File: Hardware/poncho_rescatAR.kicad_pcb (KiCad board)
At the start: 2 copper layers, 10 parts, among them P2 CONN_8, Q1 BC547

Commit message: retoques finales al esquemetico y pcb base
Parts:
- removed Q1: BC547, TO92
- removed R2: 10k, R4-LARGE_PADS
- removed R3: 680, R4-LARGE_PADS
- added BAT1: BAT_CONN, PIN_ARRAY_4x1, F.Cu at (165.3, 52.3)
- added C1: 10uF, C2V10, F.Cu at (163.9, 74.8)
- added C2: 10uF, C2V10, F.Cu at (92.2, 58.9)
- added C3: 0.1, C1, F.Cu at (162.4, 58.9)
- added C4: 0.1, C1, F.Cu at (157.3, 68.0)
- added C5: 0.1, C1, F.Cu at (103.5, 52.4)
- added C6: 0.1, C1, F.Cu at (99.5, 60.2)
- added P1: 5V_OUT, PINHEAD1-2, F.Cu at (85.2, 67.9)
- added R4: 470, R4-LARGE_PADS, F.Cu at (141.0, 62.8)
- added R5: 220, R4-LARGE_PADS, F.Cu at (150.8, 57.6)
- added U1: LM317T, TO220_VERT, F.Cu at (155.8, 62.8)
- added U2: LM7805, LM78XXV, F.Cu at (104.8, 59.0)
- CON_E-CIAA1, CON_E-CIAA2, CON_SO101, CON_SO104: footprint pin_strip_2mm_20x2 -> pin_strip_20x2
- D1: footprint LED-5MM -> LED-3MM
- P2: footprint pin_socket_2mm_8 -> pin_strip_8
- R1: value 330k -> 330
- moved R1 58.1 mm to (155.2, 85.3)
- moved D1 46.8 mm to (151.7, 91.2)
- moved P2 4.93 mm to (153.7, 109.6), turned to 270 degrees
- moved CON_E-CIAA2 4.24 mm to (90.5, 120.0)
- moved CON_E-CIAA1 3.73 mm to (161.6, 120.0)
- moved CON_SO104 2.25 mm to (122.0, 71.0)
- moved CON_SO101 2.18 mm to (122.0, 142.1), turned to 0 degrees
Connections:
- CON_E-CIAA1 pad 20: GND -> /GND
- CON_E-CIAA1 pad 22: GND -> /GND
- CON_E-CIAA1 pad 24: GND -> /GND
- CON_E-CIAA1 pad 26: GND -> /GND
- CON_E-CIAA1 pad 28: GND -> /GND
- CON_E-CIAA1 pad 30: GND -> /GND
- CON_E-CIAA1 pad 32: GND -> /GND
- CON_E-CIAA1 pad 38: GND -> /GND
- CON_E-CIAA1 pad 4: GND -> /GND
- CON_E-CIAA1 pad 40: GND -> /GND
- CON_E-CIAA2 pad 11: GND -> /GND
- CON_E-CIAA2 pad 13: GND -> /GND
- CON_E-CIAA2 pad 17: GND -> /GND
- CON_E-CIAA2 pad 19: GND -> /GND
- CON_E-CIAA2 pad 25: GND -> /GND
- CON_E-CIAA2 pad 27: GND -> /GND
- CON_E-CIAA2 pad 3: GND -> /GND
- CON_E-CIAA2 pad 37: GND -> /GND
- CON_E-CIAA2 pad 39: GND -> /GND
- CON_E-CIAA2 pad 5: GND -> /GND
- CON_E-CIAA2 pad 7: GND -> /GND
- CON_SO101 pad 11: GND -> /GND
- CON_SO101 pad 12: GND -> /GND
- CON_SO101 pad 13: GND -> /GND
- CON_SO101 pad 14: GND -> /GND
- CON_SO101 pad 19: GND -> /GND
- CON_SO101 pad 25: GND -> /GND
- CON_SO101 pad 26: GND -> /GND
- CON_SO101 pad 27: GND -> /GND
- CON_SO101 pad 28: GND -> /GND
- CON_SO101 pad 38: GND -> /GND
- CON_SO101 pad 39: GND -> /GND
- CON_SO101 pad 40: GND -> /GND
- CON_SO101 pad 5: GND -> /GND
- CON_SO104 pad 11: GND -> /GND
- CON_SO104 pad 12: GND -> /GND
- CON_SO104 pad 13: GND -> /GND
- CON_SO104 pad 14: GND -> /GND
- CON_SO104 pad 25: GND -> /GND
- CON_SO104 pad 26: GND -> /GND
- CON_SO104 pad 27: GND -> /GND
- CON_SO104 pad 28: GND -> /GND
- CON_SO104 pad 38: GND -> /GND
- CON_SO104 pad 39: GND -> /GND
- CON_SO104 pad 40: GND -> /GND
- CON_SO104 pad 5: GND -> /GND
- CON_SO104 pad 6: GND -> /GND
- CON_SO104 pad 7: GND -> /GND
- CON_SO104 pad 8: GND -> /GND
- D1 pad 1: /VCC_5V -> N-0000018
- D1 pad 2: N-000005 -> /STATUS_LED
- P2 pad 2: GND -> /GND
- P2 pad 7: GND -> /GND
- R1 pad 1: /STATUS_LED -> /VCC_3.8V
- R1 pad 2: GND -> N-0000018
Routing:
- net /VCC_5V: track 104.9 -> 0.00 mm
- net /VCC_3.8V: track 0.00 -> 104.1 mm
- net VCC: track 0.00 -> 72.6 mm
- net /RS232_RXD: track 98.9 -> 61.6 mm
- net /STATUS_LED: track 6.41 -> 37.3 mm
- net /RS232_TXD: track 42.4 -> 66.6 mm
- net N-000003: track 0.00 -> 21.8 mm
- net N-000002: track 0.00 -> 14.6 mm
- net /I2C_SCL: track 17.0 -> 28.6 mm
- net GND: track 10.5 -> 0.00 mm
- net N-000005: track 9.38 -> 0.00 mm
- net N-000007: track 5.64 -> 0.00 mm
- net /GE864_ON_OFF: track 99.8 -> 105.4 mm
- net N-000009: track 4.02 -> 0.00 mm
- net N-0000018: track 0.00 -> 3.63 mm
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
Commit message: perfeccionando el  pcb
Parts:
- C1, C2: footprint C2V10 -> C1V5
- moved C4 14.0 mm to (162.7, 55.1), turned to 90 degrees
- moved C1 13.1 mm to (163.9, 61.6), turned to 270 degrees
- moved R4 9.59 mm to (139.7, 53.2)
- moved R5 9.43 mm to (141.6, 60.0)
- moved C3 8.90 mm to (156.5, 52.3)
- moved U1 6.73 mm to (155.2, 56.0)
- moved BAT1 6.20 mm to (168.4, 57.6), turned to 270 degrees
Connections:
- U1 pad 2: VCC -> /VCC_3.8V
- U1 pad 3: /VCC_3.8V -> VCC
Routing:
- net /VCC_3.8V: track 104.1 -> 124.5 mm
- net /VCC_5V: track 0.00 -> 16.5 mm
- net N-000002: track 14.6 -> 22.3 mm
- net N-000003: track 21.8 -> 24.7 mm
- net VCC: track 72.6 -> 75.5 mm
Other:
- net class Default: clearance 0.7 -> 0.8
- net class Power added: clearance 0.8, trace_width 1, via_dia 0.889, via_drill 0.635
- rule trace_clearance: 0.7 -> 0.8

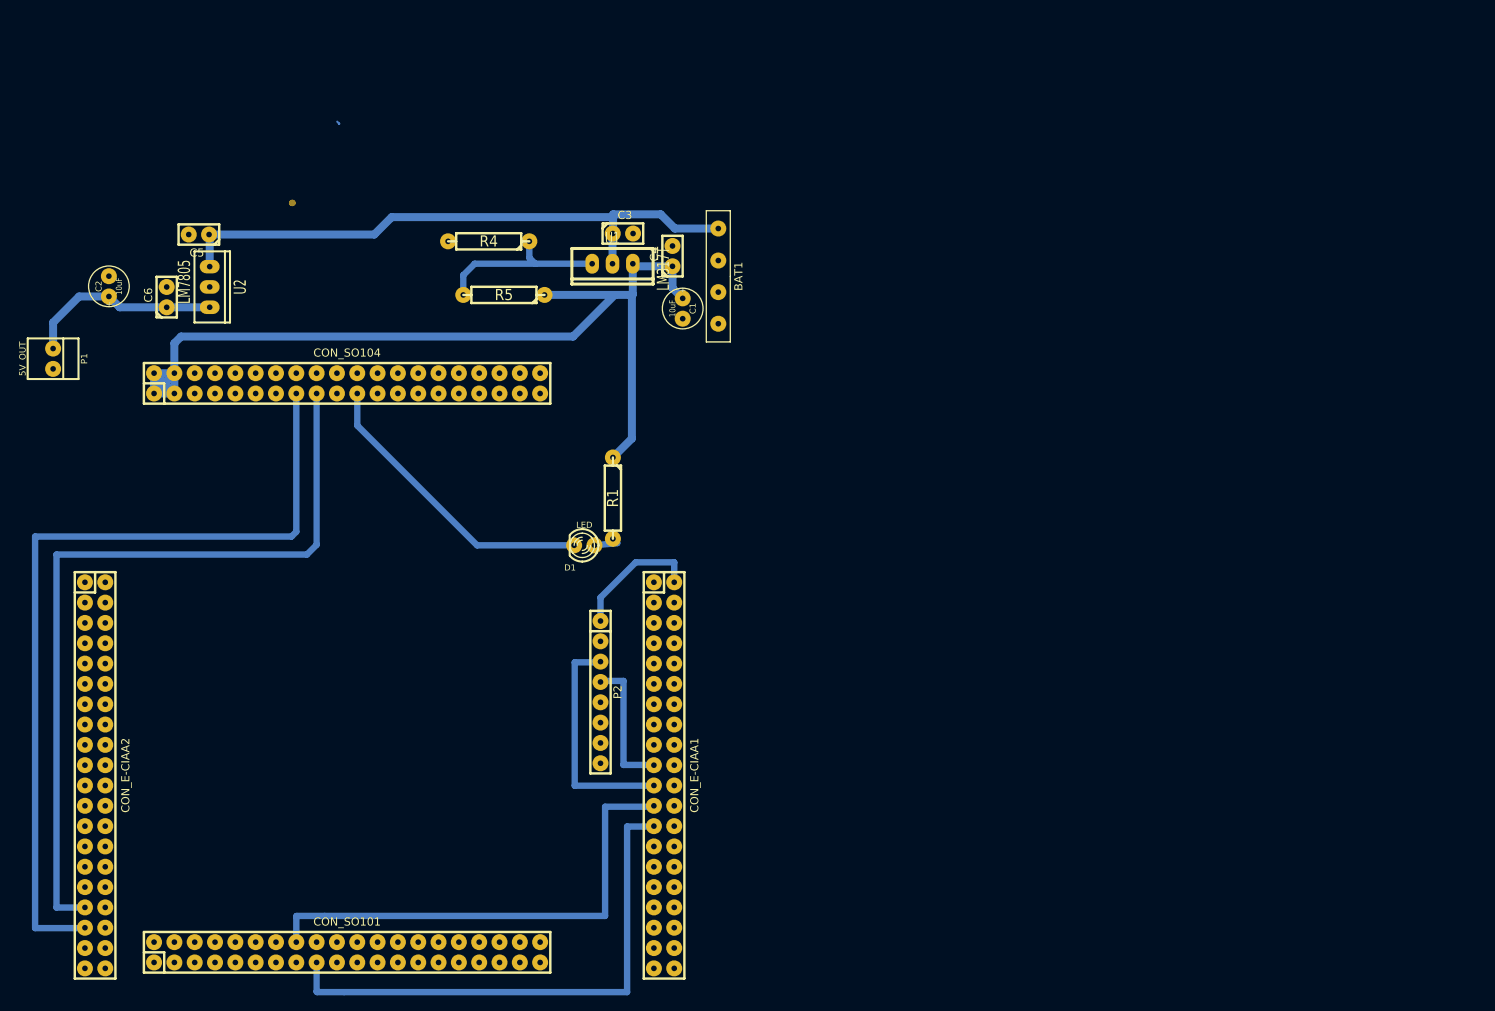
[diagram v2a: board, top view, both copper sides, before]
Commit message: mas retoques al pcb, consideracion del boton de reset y los disipadores
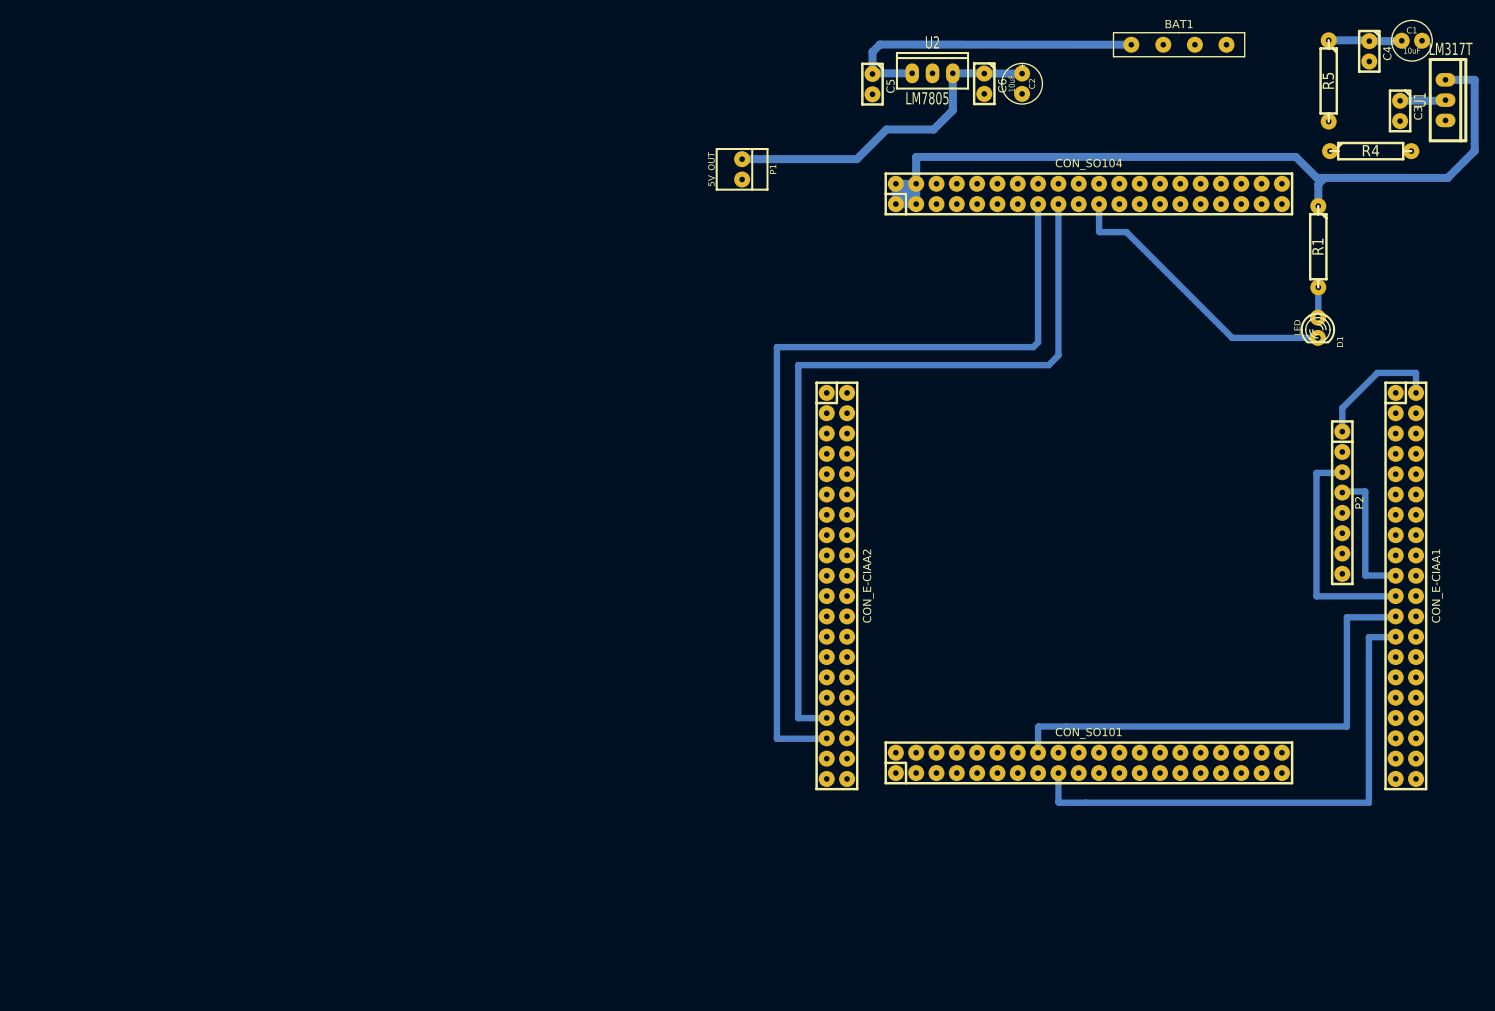
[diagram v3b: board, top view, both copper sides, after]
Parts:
- moved C2 116.9 mm to (206.4, 33.5), turned to 270 degrees
- moved R4 110.8 mm to (249.9, 42.0), turned to 0 degrees
- moved R5 106.5 mm to (244.7, 33.2), turned to 270 degrees
- moved U1 106.1 mm to (259.3, 35.6), turned to 0 degrees
- moved C6 105.6 mm to (201.7, 33.5), turned to 270 degrees
- moved C3 98.4 mm to (253.6, 37.0), turned to 270 degrees
- moved C1 97.1 mm to (255.1, 28.2), turned to 0 degrees
- moved CON_E-CIAA1 95.7 mm to (254.3, 96.3)
- moved CON_E-CIAA2 95.7 mm to (183.2, 96.3)
- moved CON_SO101 95.7 mm to (214.7, 118.4)
- moved CON_SO104 95.7 mm to (214.7, 47.3)
- moved P2 95.7 mm to (246.4, 85.9)
- moved D1 95.6 mm to (243.3, 64.0), turned to 270 degrees
- moved U2 94.2 mm to (195.2, 32.2), turned to 90 degrees
- moved R1 93.6 mm to (243.4, 53.9)
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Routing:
- net VCC: track 75.5 -> 46.2 mm
- net N-000002: track 22.3 -> 0.00 mm
- net N-000003: track 24.7 -> 42.2 mm
- net /VCC_3.8V: track 124.5 -> 118.6 mm
- net /STATUS_LED: track 37.3 -> 36.3 mm
- net (no net): track 0.61 -> 0.00 mm
